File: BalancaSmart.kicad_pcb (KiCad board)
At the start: 2 copper layers, 100 x 100 mm, 56 parts, among them J1 Load Cell, J2 Barrel_Jack, Q1 PMOS, Q2 NMOS, Q3 NMOS, Q4 S8050, SW1 SW_Push, U1 HX711-Mod, U2 ADS1115-module, U3 HX-2S-JH20, U4 XL4015

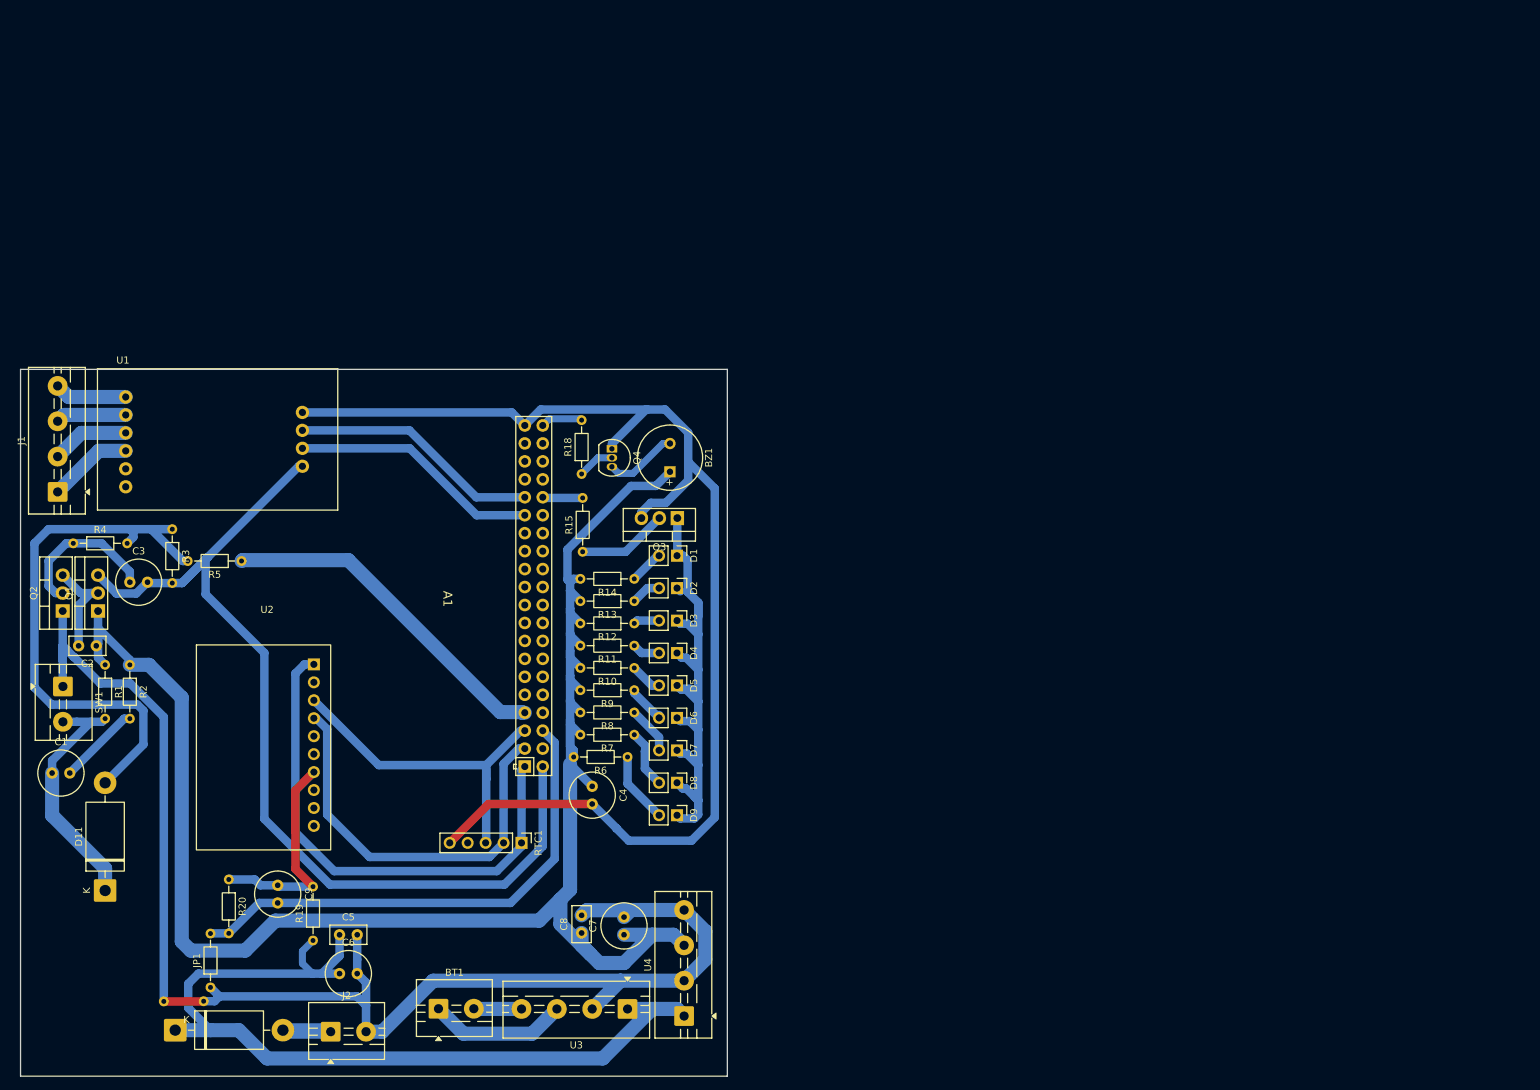
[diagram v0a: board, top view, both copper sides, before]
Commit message: correção da orientação da raspberry e ADS1115 no layout da PCB e inicio do retrabalho do roteamento das trilhas
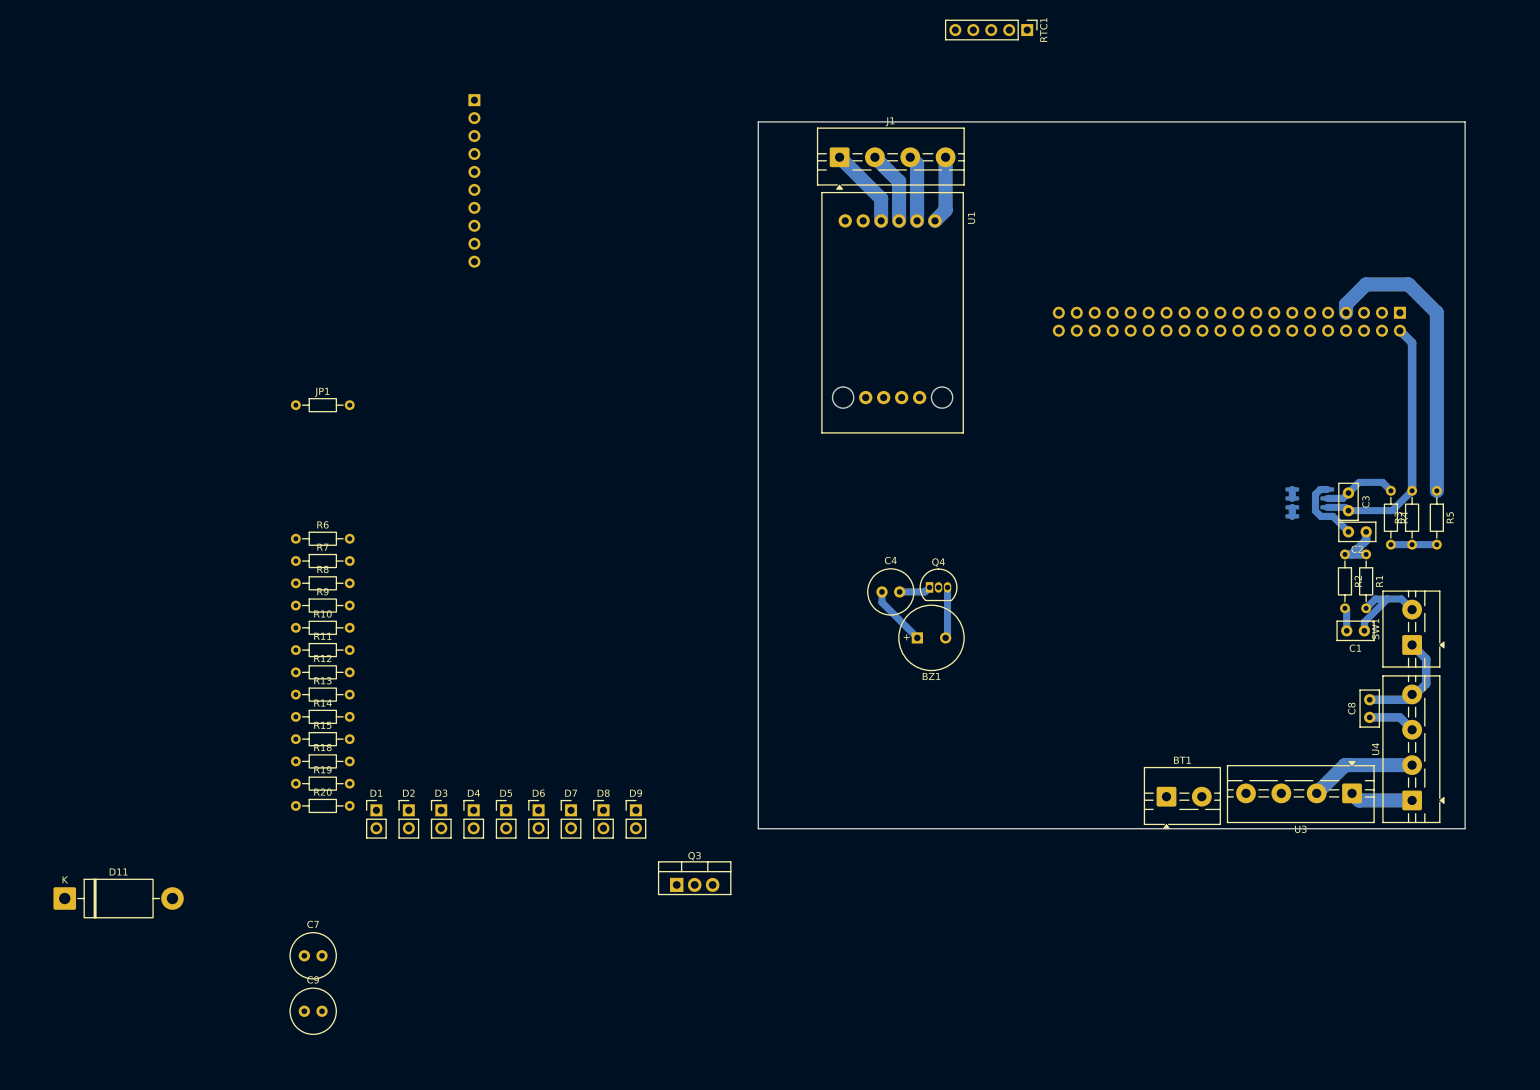
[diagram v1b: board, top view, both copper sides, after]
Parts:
- removed ? (x2): , 
- removed C5: 100nF, Capacitor_THT:C_Disc_D5.0mm_W2.5mm_P2.50mm
- removed C6: 470uF, Capacitor_THT:C_Radial_D6.3mm_H7.0mm_P2.50mm
- removed D10: 1N5822, Diode_THT:D_DO-201AD_P15.24mm_Horizontal
- removed J2: Barrel_Jack, TerminalBlock:TerminalBlock_MaiXu_MX126-5.0-02P_1x02_P5.00mm
- removed Q1: PMOS, Package_TO_SOT_THT:TO-220-3_Vertical
- removed Q2: NMOS, Package_TO_SOT_THT:TO-220-3_Vertical
- added Q5: IRF7309PBF, Package_SO:SOIC-8_3.9x4.9mm_P1.27mm, B.Cu at (245.5, 94.9)
- A1: footprint Raspberry_Pi_Zero_v.1.3_Hat:RASPI_ZERO_FULL -> Module:Raspberry_Pi_Zero_Socketed_THT_FaceDown_MountingHoles; moved to B.Cu
- C1, C3: footprint Capacitor_THT:C_Radial_D6.3mm_H7.0mm_P2.50mm -> Capacitor_THT:C_Disc_D5.0mm_W2.5mm_P2.50mm
- U1: footprint HX711_mod:HX711_module -> project_library:HX711_module
- U2: moved to B.Cu
- moved SW1 191.0 mm to (260.0, 115.0), turned to 90 degrees
- moved C1 186.8 mm to (253.2, 113.0), turned to 180 degrees
- moved R4 186.6 mm to (257.0, 93.2), turned to -90 degrees
- moved C2 180.4 mm to (253.5, 99.0)
- moved R1 179.1 mm to (253.5, 102.2)
- moved R3 175.4 mm to (260.0, 100.8), turned to 90 degrees
- moved C3 172.9 mm to (251.0, 93.5), turned to -90 degrees
- moved R2 172.6 mm to (250.5, 102.2)
- moved R5 169.4 mm to (263.5, 93.2), turned to -90 degrees
- moved A1 149.2 mm to (258.3, 68.0), turned to 90 degrees
- moved RTC1 135.4 mm to (205.5, 28.0)
- moved J1 120.3 mm to (179.0, 46.0), turned to 0 degrees
- moved C8 115.6 mm to (254.0, 125.2)
- moved U4 107.4 mm to (260.0, 137.0)
- moved BT1 107.3 mm to (225.2, 136.5)
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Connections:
- C1 pad 2: Net-(C1-Pad2) -> Net-(Q5A-S1)
- C2 pad 2: Net-(Q1-G) -> Net-(Q5A-S1)
- C7 pad 2: P- -> GND
- C8 pad 2: P- -> GND
- JP1 pad 1: P- -> GND
- R2 pad 2: Net-(C1-Pad2) -> Net-(Q5A-S1)
- SW1 pad 1: P- -> GND
- U2 pad 2: (no net) -> Earth
- U4 pad 4: P- -> GND
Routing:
- net Earth: track 248.5 -> 4.50 mm
- net +5V: track 249.8 -> 23.6 mm
- net P-: track 200.0 -> 15.2 mm
- net P+: track 122.8 -> 8.91 mm
- net pino 5v rasp: track 140.1 -> 36.7 mm
- net Net-(D1-K): track 75.9 -> 0.00 mm
- net Net-(D11-A): track 79.6 -> 6.50 mm
- net +3V3: track 72.8 -> 0.00 mm
- net I2C SDA: track 57.9 -> 0.00 mm
- net I2C SCL: track 48.3 -> 0.00 mm
- net DAT HX711: track 35.4 -> 0.00 mm
- net CLK HX711: track 35.4 -> 0.00 mm
- net Net-(U2-A0): track 30.8 -> 0.00 mm
- net Net-(D11-K): track 35.4 -> 13.9 mm
- net Net-(BT1-+): track 19.7 -> 0.00 mm
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
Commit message: trilhas
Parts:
- removed BT1: Battery, TerminalBlock:TerminalBlock_MaiXu_MX126-5.0-02P_1x02_P5.00mm
- removed C1: 1uF, Capacitor_THT:C_Disc_D5.0mm_W2.5mm_P2.50mm
- removed C2: 0.1uF, Capacitor_THT:C_Disc_D5.0mm_W2.5mm_P2.50mm
- removed C3: 10uF, Capacitor_THT:C_Disc_D5.0mm_W2.5mm_P2.50mm
- removed C4: 10uF, Capacitor_THT:C_Radial_D6.3mm_H7.0mm_P2.50mm
- removed D1, D2, D3, D4, D5, D6, D7, D8, D9: LED, Connector_PinHeader_2.54mm:PinHeader_1x02_P2.54mm_Vertical
- removed D11: 1N5400, Diode_THT:D_DO-201AD_P15.24mm_Horizontal
- removed JP1: Jumper_2_Bridged, Resistor_THT:R_Axial_DIN0204_L3.6mm_D1.6mm_P7.62mm_Horizontal
- removed Q3: NMOS, Package_TO_SOT_THT:TO-220-3_Vertical
- removed Q5: IRF7309PBF, Package_SO:SOIC-8_3.9x4.9mm_P1.27mm
- removed R10, R11, R12, R13, R14, R7, R8, R9: 100, Resistor_THT:R_Axial_DIN0204_L3.6mm_D1.6mm_P7.62mm_Horizontal
- removed R15: 1k, Resistor_THT:R_Axial_DIN0204_L3.6mm_D1.6mm_P7.62mm_Horizontal
- added J2: NeoPixel Ring Light, TerminalBlock:TerminalBlock_MaiXu_MX126-5.0-03P_1x03_P5.00mm, F.Cu at (107.2, 85.5)
- added Q1: IRF9540N, Package_TO_SOT_THT:TO-220-3_Vertical, F.Cu at (248.5, 81.1)
- added U5: Optocoupler_DC_PhotoNPN_AKEC, Package_DIP:DIP-4_W7.62mm_Socket_LongPads, F.Cu at (243.9, 109.5)
- R1: value 10k -> 1M
- R3: value 100k -> 1k
- R4: value 300k -> 1k
- R5: value 1k -> 2k
- R6: value 100 -> 1k
- U3: footprint TerminalBlock:TerminalBlock_MaiXu_MX126-5.0-04P_1x04_P5.00mm -> TerminalBlock:TerminalBlock_MaiXu_MX126-5.0-02P_1x02_P5.00mm
- moved R5 169.7 mm to (94.4, 107.0), turned to 0 degrees
- moved R4 163.0 mm to (94.4, 103.8), turned to 0 degrees
- moved R1 159.3 mm to (94.4, 94.3), turned to 0 degrees
- moved R2 156.2 mm to (94.4, 97.5), turned to 0 degrees
- moved R18 154.5 mm to (254.2, 104.3), turned to 90 degrees
- moved C7 148.7 mm to (248.5, 127.0)
- moved R20 132.0 mm to (233.0, 121.0), turned to -90 degrees
- moved R19 128.0 mm to (229.9, 128.6), turned to 90 degrees
- moved C9 78.7 mm to (148.6, 102.5)
- moved J1 67.8 mm to (192.0, 112.5), turned to 180 degrees
- moved BZ1 63.4 mm to (126.7, 116.3)
- moved RTC1 57.7 mm to (253.1, 60.7), turned to 0 degrees
- moved Q4 47.1 mm to (146.5, 120.2)
- moved R3 29.0 mm to (261.5, 129.8)
- moved U3 26.0 mm to (225.5, 135.0), turned to 0 degrees
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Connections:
- A1 pad 11: unconnected-(A1-GP17-Pad11) -> Ring Light
- A1 pad 35: unconnected-(A1-GP19-Pad35) -> button pin
- A1 pad 4: unconnected-(A1-+5V-Pad4) -> pino 5v rasp
- BZ1 pad 1: +5V -> pino 5v rasp
- C7 pad 2: GND -> Earth
- C8 pad 2: GND -> Earth
- R1 pad 2: Net-(D11-K) -> Net-(Q1-G)
- R2 pad 1: +5V -> Net-(Q1-G)
- R2 pad 2: Net-(Q5A-S1) -> Net-(R2-Pad2)
- R3 pad 1: Net-(D11-A) -> +5V
- R3 pad 2: pino 5v rasp -> Net-(R2-Pad2)
- R4 pad 1: Net-(Q5A-G1) -> Net-(R2-Pad2)
- R4 pad 2: Net-(D11-A) -> Sinal de desligamento
- R5 pad 2: Net-(D11-A) -> Earth
- R6 pad 2: +5V -> button pin
- SW1 pad 1: GND -> Earth
- SW1 pad 2: Net-(D11-K) -> Net-(R2-Pad2)
- U4 pad 4: GND -> Earth
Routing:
- net I2C SCL: track 0.00 -> 43.2 mm
- net Sinal de desligamento: track 42.0 -> 0.00 mm
- net Earth: track 4.50 -> 46.3 mm
- net pino 5v rasp: track 36.7 -> 0.00 mm
- net I2C SDA: track 0.00 -> 28.7 mm
- net GND: track 16.5 -> 0.00 mm
- net +3V3: track 0.00 -> 14.4 mm
- net Net-(D11-K): track 13.9 -> 0.00 mm
- net Net-(Q5A-S1): track 13.5 -> 0.00 mm
- net P+: track 8.91 -> 22.2 mm
- net +5V: track 23.6 -> 36.2 mm
- net Net-(Q5A-G1): track 10.4 -> 0.00 mm
- net Net-(BZ1--): track 7.25 -> 0.00 mm
- net Net-(D11-A): track 6.50 -> 0.00 mm
- net Net-(R2-Pad2): track 0.00 -> 4.95 mm
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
